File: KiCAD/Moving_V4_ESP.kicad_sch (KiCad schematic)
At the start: 79 parts, among them J1 Vin_1, J2 Vin_2, J3 Power_SW, J4 USB_B_Micro, J5 MOTOR_R, J6 Motor_L, J7 Conn_01x04_Pin, J8 Conn_01x04_Pin, J9 Vin_XT, Q1 U4_ALT2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

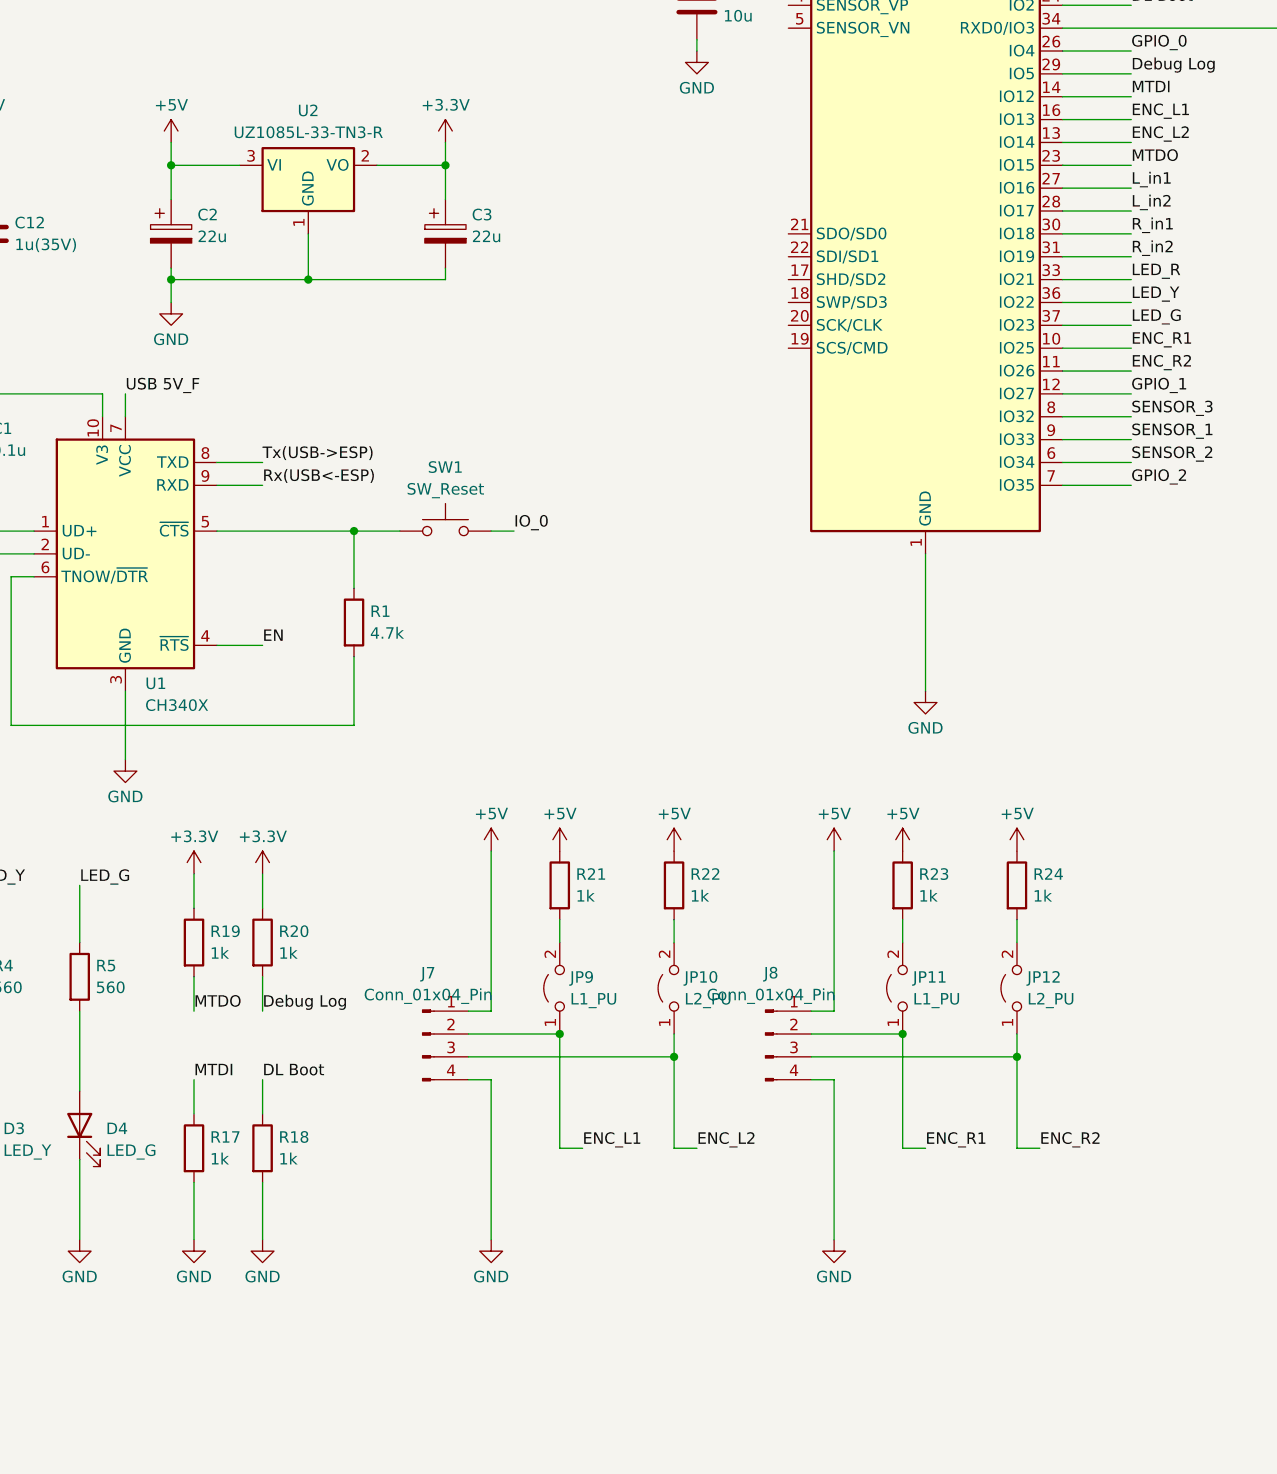
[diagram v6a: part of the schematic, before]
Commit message: エンコーダ入力回路にレベルシフタを追加
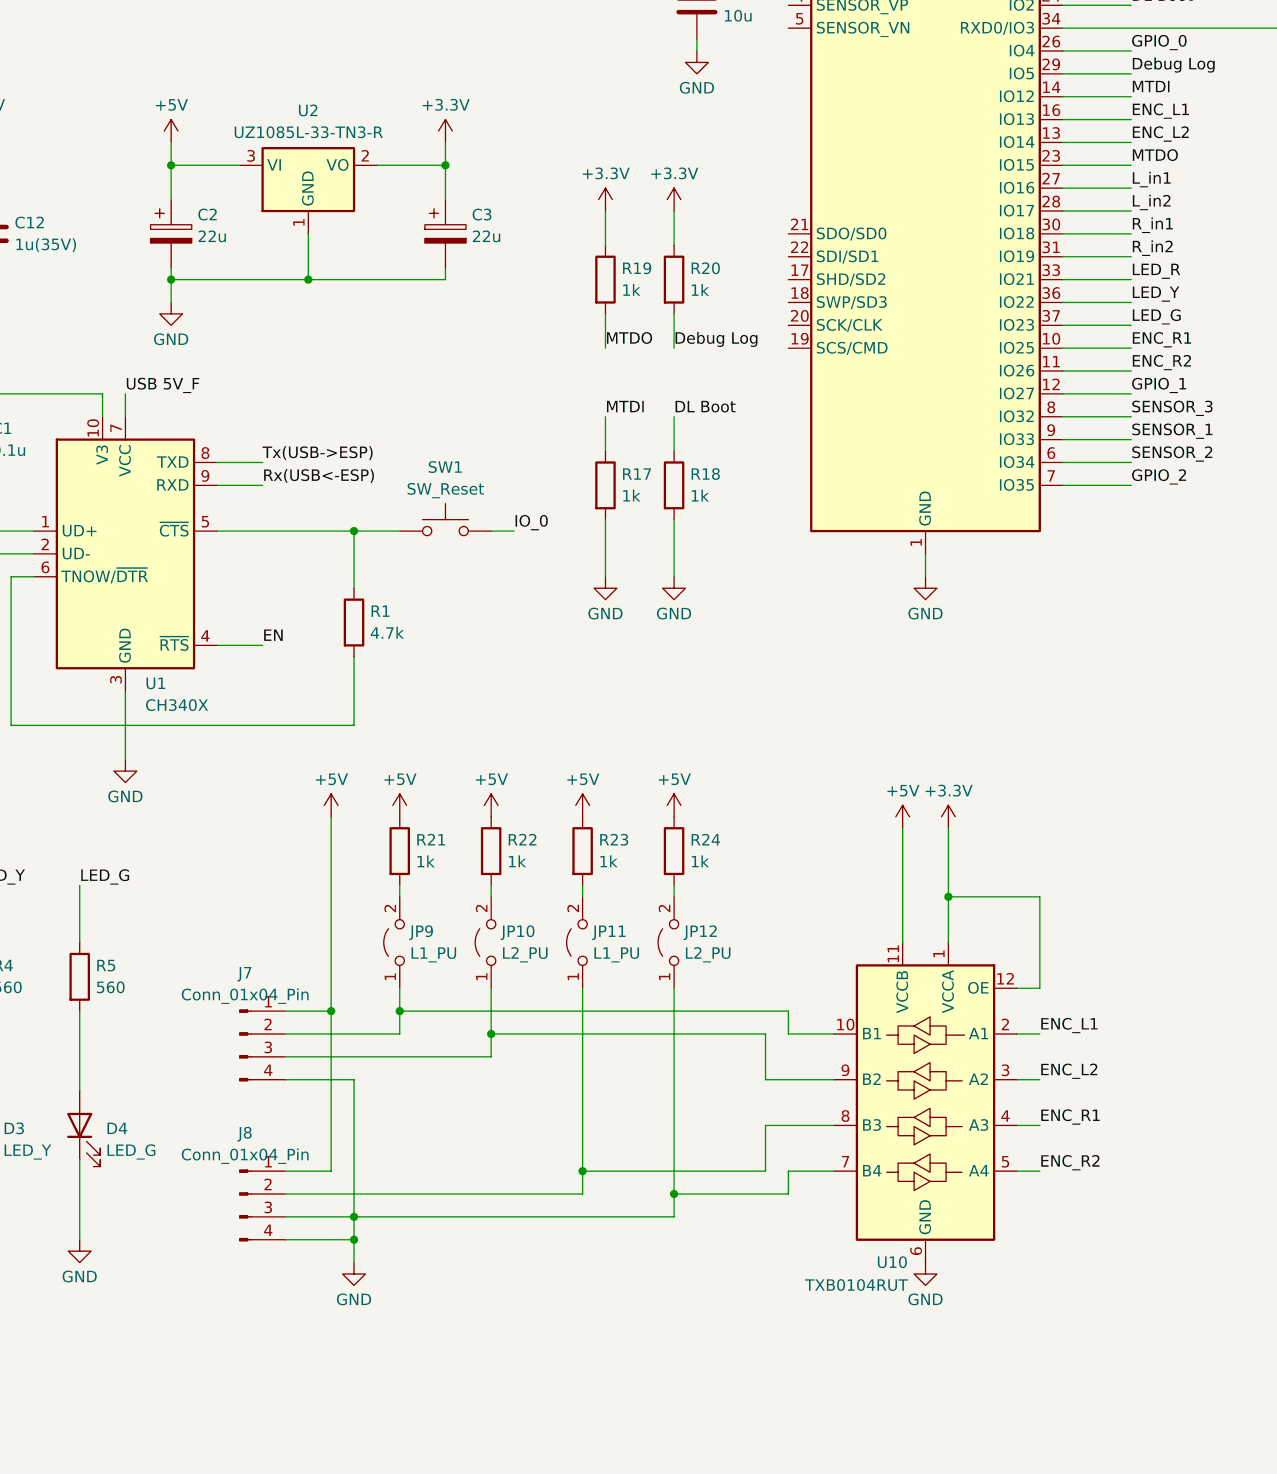
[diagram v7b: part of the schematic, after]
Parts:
- added U10: TXB0104RUT, Package_DFN_QFN:Texas_R-PUQFN-N12, symbol Logic_LevelTranslator:TXB0104RUT
- J7, J8: footprint (none) -> Connector_JST:JST_PH_B4B-PH-K_1x04_P2.00mm_Vertical
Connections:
- net +3.3V: now also U10.1 (VCCA), U10.12 (OE)
- net +5V: now also U10.11 (VCCB)
- net ENC_L1: now also U10.2 (A1); no longer J7.2 (Pin_2), JP9.1 (A)
- net ENC_L2: now also U10.3 (A2); no longer J7.3 (Pin_3), JP10.1 (A)
- net ENC_R1: now also U10.4 (A3); no longer J8.2 (Pin_2), JP11.1 (A)
- net ENC_R2: now also U10.5 (A4); no longer J8.3 (Pin_3), JP12.1 (A)
- net GND: now also J8.3 (Pin_3), JP12.1 (A), U10.6 (GND), U10.7 (B4)
- new net: J8.2 (Pin_2), JP11.1 (A), U10.8 (B3)
- new net: J7.2 (Pin_2), JP9.1 (A), U10.10 (B1)
- new net: J7.3 (Pin_3), JP10.1 (A), U10.9 (B2)
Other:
- moved on the sheet: J7, J8, JP10, JP11, JP12, JP9, R17, R18, R19, R20, R21, R22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

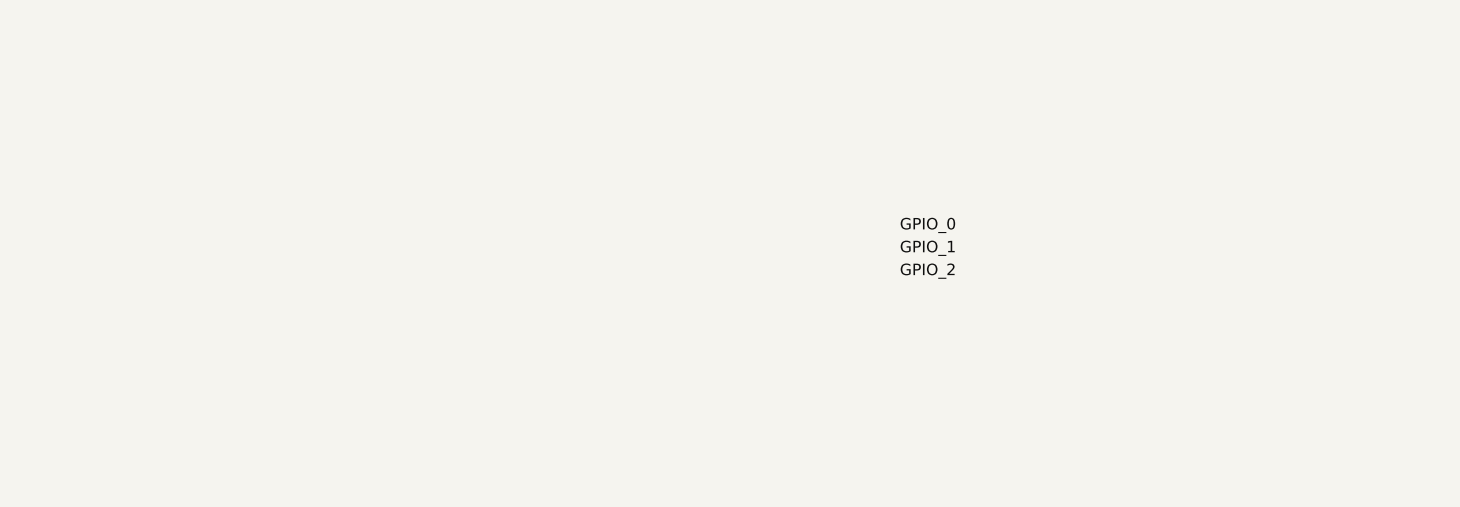
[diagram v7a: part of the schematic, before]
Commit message: 汎用IOを追加。回路図はいったんシート外に記載。GPIO3にはDebug Logピンを使用
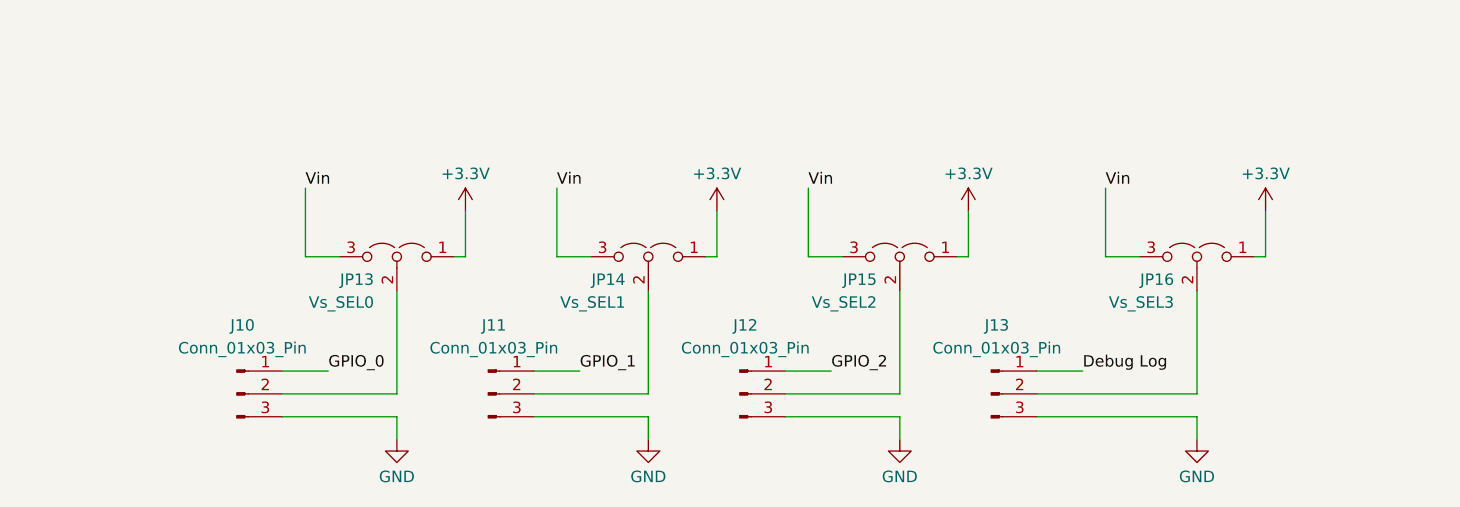
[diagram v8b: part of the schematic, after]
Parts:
- added J10, J11, J12, J13: Conn_01x03_Pin, symbol Connector:Conn_01x03_Pin
- added JP13: Vs_SEL0, Jumper:SolderJumper-3_P1.3mm_Open_RoundedPad1.0x1.5mm, symbol Jumper:Jumper_3_Open
- added JP14: Vs_SEL1, Jumper:SolderJumper-3_P1.3mm_Open_RoundedPad1.0x1.5mm, symbol Jumper:Jumper_3_Open
- added JP15: Vs_SEL2, Jumper:SolderJumper-3_P1.3mm_Open_RoundedPad1.0x1.5mm, symbol Jumper:Jumper_3_Open
- added JP16: Vs_SEL3, Jumper:SolderJumper-3_P1.3mm_Open_RoundedPad1.0x1.5mm, symbol Jumper:Jumper_3_Open
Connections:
- net +3.3V: now also JP13.1 (A), JP14.1 (A), JP15.1 (A), JP16.1 (A)
- net Debug Log: now also J13.1 (Pin_1)
- net GND: now also J10.3 (Pin_3), J11.3 (Pin_3), J12.3 (Pin_3), J13.3 (Pin_3)
- net GPIO_0: now also J10.1 (Pin_1)
- net GPIO_1: now also J11.1 (Pin_1)
- net GPIO_2: now also J12.1 (Pin_1)
- net Vin: now also JP13.3 (B), JP14.3 (B), JP15.3 (B), JP16.3 (B)
- new net: J11.2 (Pin_2), JP14.2 (C)
- new net: J12.2 (Pin_2), JP15.2 (C)
- new net: J13.2 (Pin_2), JP16.2 (C)
- new net: J10.2 (Pin_2), JP13.2 (C)
